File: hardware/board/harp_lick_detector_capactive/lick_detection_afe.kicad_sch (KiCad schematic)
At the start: 38 parts, among them J1 Conn_Coaxial, J3 Conn_Triaxial, U13 ADS7049, U6 LTC6263, U7 LTC6268xS8-10, U8 REF3433QDBVRQ1

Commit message: update footprints; populate bom
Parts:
- C22, C23, C27, C29: Link https://www.digikey.com/en/products/detail/murata-electronics/GRM188R61E106KA73J/9887674 -> https://www.digikey.com/en/products/detail/murata-electronics/GRM188R61E106KA73D/9867943; Manufacturer Number GRM188R61E106KA73J -> GRM188R61E106KA73D; Rated Voltage 10 -> 25V
- C28: footprint Capacitor_SMD:C_0402_1005Metric_Pad0.74x0.62mm_HandSolder -> Capacitor_SMD:C_0402_1005Metric
- R15: Link (none) -> https://www.digikey.com/en/products/detail/yageo/RT0402FRE0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; Manufacturer (none) -> Yageo; Manufacturer Number (none) -> RT0402FRE07100RL; Tolerance (none) -> 1%
- U7: Link (none) -> https://www.digikey.com/en/products/detail/analog-devices-i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; Manufacturer (none) -> Analog Devices Inc.; Manufacturer Number (none) -> LTC6268IS8-10#PBF
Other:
- note added: "TODO: J1 TVS Diode for static protection."
- company: (none) -> The Allen Institute for Neural Dynamics
- title: (none) -> Lickety Split Capacitive Lick Detector
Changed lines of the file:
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@@
 (kicad_sch (version 20230121) (generator eeschema)
   (paper "A4")
+  (title_block
+    (title "Lickety Split Capacitive Lick Detector")
+    (date "2023-09-01")
+    (rev "0.5")
+    (company "The Allen Institute for Neural Dynamics")
+  )
   (junction (at 247.65 28.575) (diameter 0) (color 0 0 0 0)
   )
@@
     (at 20.955 83.185 0)
     (effects (font (size 1.27 1.27)) (justify left bottom))
+  )
+  (text "TODO: J1 TVS Diode for static protection." (at 201.93 140.335 0)
+    (effects (font (size 2 2) (thickness 0.4) bold) (justify left bottom))
   )
   (text "TODO: consider common mode choke for connector inputs.\n3-line: EXC-16CT350U"
@@
       (effects (font (size 1.27 1.27)) hide)
     )
+    (property "Manufacturer Number" "LTC6268IS8-10#PBF" (at 109.22 97.155 0)
+      (effects (font (size 1.27 1.27)) hide)
+    )
+    (property "Manufacturer" "Analog Devices Inc." (at 109.22 97.155 0)
+      (effects (font (size 1.27 1.27)) hide)
+    )
+    (property "Link" "https://www.digikey.com/en/products/detail/analog-devices-inc/LTC6268IS8-10-PBF/5253539" (at 109.22 97.155 0)
+      (effects (font (size 1.27 1.27)) hide)
+    )
     (pin "1")
     (pin "2")
@@
       (effects (font (size 1.27 1.27)) hide)
     )
-    (property "Datasheet" "~" (at 92.71 97.155 0)
+    (property "Datasheet" "n/a" (at 92.71 97.155 0)
+      (effects (font (size 1.27 1.27)) hide)
+    )
+    (property "Link" "https://www.digikey.com/en/products/detail/yageo/RT0402FRE07100RL/1071699" (at 92.71 97.155 0)
+      (effects (font (size 1.27 1.27)) hide)
+    )
+    (property "Manufacturer" "Yageo" (at 92.71 97.155 0)
+      (effects (font (size 1.27 1.27)) hide)
+    )
+    (property "Manufacturer Number" "RT0402FRE07100RL" (at 92.71 97.155 0)
+      (effects (font (size 1.27 1.27)) hide)
+    )
+    (property "Tolerance" "1%" (at 92.71 97.155 0)
       (effects (font (size 1.27 1.27)) hide)
     )
@@
       (effects (font (size 1.27 1.27)) hide)
     )
-    (property "Datasheet" "https://search.murata.co.jp/Ceramy/image/img/A01X/G101/ENG/GRM188R61E106KA73-01A.pdf" (at 125.73 179.07 0)
-      (effects (font (size 1.27 1.27)) hide)
-    )
-    (property "Link" "https://www.digikey.com/en/products/detail/murata-electronics/GRM188R61E106KA73J/9887674" (at 125.73 179.07 0)
+    (property "Datasheet" "https://search.murata.co.jp/Ceramy/image/img/A01X/G101/ENG/GRM188R61E106KA73-01.pdf" (at 125.73 179.07 0)
+      (effects (font (size 1.27 1.27)) hide)
+    )
+    (property "Link" "https://www.digikey.com/en/products/detail/murata-electronics/GRM188R61E106KA73D/9867943" (at 125.73 179.07 0)
       (effects (font (size 1.27 1.27)) hide)
     )
@@
       (effects (font (size 1.27 1.27)) hide)
     )
-    (property "Manufacturer Number" "GRM188R61E106KA73J" (at 125.73 179.07 0)
-      (effects (font (size 1.27 1.27)) hide)
-    )
-    (property "Rated Voltage" "10" (at 125.73 179.07 0)
+    (property "Manufacturer Number" "GRM188R61E106KA73D" (at 125.73 179.07 0)
+      (effects (font (size 1.27 1.27)) hide)
+    )
+    (property "Rated Voltage" "25V" (at 125.73 179.07 0)
       (effects (font (size 1.27 1.27)) hide)
     )
@@
       (effects (font (size 1.27 1.27)) (justify left))
     )
-    (property "Footprint" "Capacitor_SMD:C_0402_1005Metric_Pad0.74x0.62mm_HandSolder" (at 115.8748 175.26 0)
+    (property "Footprint" "Capacitor_SMD:C_0402_1005Metric" (at 115.8748 175.26 0)
       (effects (font (size 1.27 1.27)) hide)
     )
@@
       (effects (font (size 1.27 1.27)) hide)
     )
-    (property "Datasheet" "https://search.murata.co.jp/Ceramy/image/img/A01X/G101/ENG/GRM188R61E106KA73-01A.pdf" (at 32.385 172.72 0)
-      (effects (font (size 1.27 1.27)) hide)
-    )
-    (property "Link" "https://www.digikey.com/en/products/detail/murata-electronics/GRM188R61E106KA73J/9887674" (at 32.385 172.72 0)
+    (property "Datasheet" "https://search.murata.co.jp/Ceramy/image/img/A01X/G101/ENG/GRM188R61E106KA73-01.pdf" (at 32.385 172.72 0)
+      (effects (font (size 1.27 1.27)) hide)
+    )
+    (property "Link" "https://www.digikey.com/en/products/detail/murata-electronics/GRM188R61E106KA73D/9867943" (at 32.385 172.72 0)
       (effects (font (size 1.27 1.27)) hide)
     )
@@
       (effects (font (size 1.27 1.27)) hide)
     )
-    (property "Manufacturer Number" "GRM188R61E106KA73J" (at 32.385 172.72 0)
-      (effects (font (size 1.27 1.27)) hide)
-    )
-    (property "Rated Voltage" "10" (at 32.385 172.72 0)
+    (property "Manufacturer Number" "GRM188R61E106KA73D" (at 32.385 172.72 0)
+      (effects (font (size 1.27 1.27)) hide)
+    )
+    (property "Rated Voltage" "25V" (at 32.385 172.72 0)
       (effects (font (size 1.27 1.27)) hide)
     )
@@
       (effects (font (size 1.27 1.27)) hide)
     )
-    (property "Datasheet" "https://search.murata.co.jp/Ceramy/image/img/A01X/G101/ENG/GRM188R61E106KA73-01A.pdf" (at 32.385 184.15 0)
-      (effects (font (size 1.27 1.27)) hide)
-    )
-    (property "Link" "https://www.digikey.com/en/products/detail/murata-electronics/GRM188R61E106KA73J/9887674" (at 32.385 184.15 0)
+    (property "Datasheet" "https://search.murata.co.jp/Ceramy/image/img/A01X/G101/ENG/GRM188R61E106KA73-01.pdf" (at 32.385 184.15 0)
+      (effects (font (size 1.27 1.27)) hide)
+    )
+    (property "Link" "https://www.digikey.com/en/products/detail/murata-electronics/GRM188R61E106KA73D/9867943" (at 32.385 184.15 0)
       (effects (font (size 1.27 1.27)) hide)
     )
@@
       (effects (font (size 1.27 1.27)) hide)
     )
-    (property "Manufacturer Number" "GRM188R61E106KA73J" (at 32.385 184.15 0)
-      (effects (font (size 1.27 1.27)) hide)
-    )
-    (property "Rated Voltage" "10" (at 32.385 184.15 0)
+    (property "Manufacturer Number" "GRM188R61E106KA73D" (at 32.385 184.15 0)
+      (effects (font (size 1.27 1.27)) hide)
+    )
+    (property "Rated Voltage" "25V" (at 32.385 184.15 0)
       (effects (font (size 1.27 1.27)) hide)
     )
@@
       (effects (font (size 1.27 1.27)) hide)
     )
-    (property "Datasheet" "https://search.murata.co.jp/Ceramy/image/img/A01X/G101/ENG/GRM188R61E106KA73-01A.pdf" (at 99.06 179.07 0)
-      (effects (font (size 1.27 1.27)) hide)
-    )
-    (property "Link" "https://www.digikey.com/en/products/detail/murata-electronics/GRM188R61E106KA73J/9887674" (at 99.06 179.07 0)
+    (property "Datasheet" "https://search.murata.co.jp/Ceramy/image/img/A01X/G101/ENG/GRM188R61E106KA73-01.pdf" (at 99.06 179.07 0)
+      (effects (font (size 1.27 1.27)) hide)
+    )
+    (property "Link" "https://www.digikey.com/en/products/detail/murata-electronics/GRM188R61E106KA73D/9867943" (at 99.06 179.07 0)
       (effects (font (size 1.27 1.27)) hide)
     )
@@
       (effects (font (size 1.27 1.27)) hide)
     )
-    (property "Manufacturer Number" "GRM188R61E106KA73J" (at 99.06 179.07 0)
-      (effects (font (size 1.27 1.27)) hide)
-    )
-    (property "Rated Voltage" "10" (at 99.06 179.07 0)
-      (effects (font (size 1.27 1.27)) hide)
-    )
+    (property "Manufacturer Number" "GRM188R61E106KA73D" (at 99.06 179.07 0)
+      (effects (font (size 1.27 1.27)) hide)
+    )
+    (property "Rated Voltage" "25V" (at 99.06 179.07 0)
+      (effects (font (size 1.27 1.27)) hide)
+    )

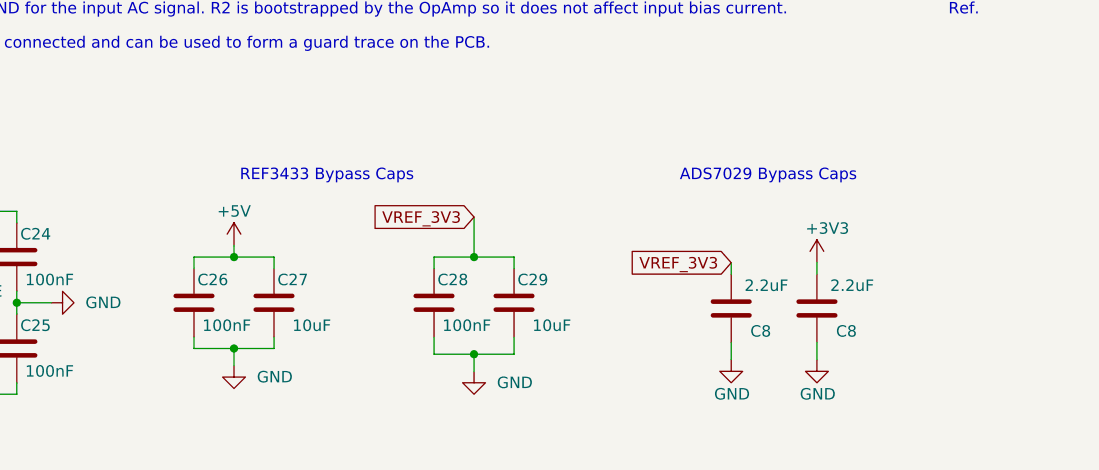
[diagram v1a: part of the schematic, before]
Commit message: consolidate components; add extra decoupling cap to voltage divider
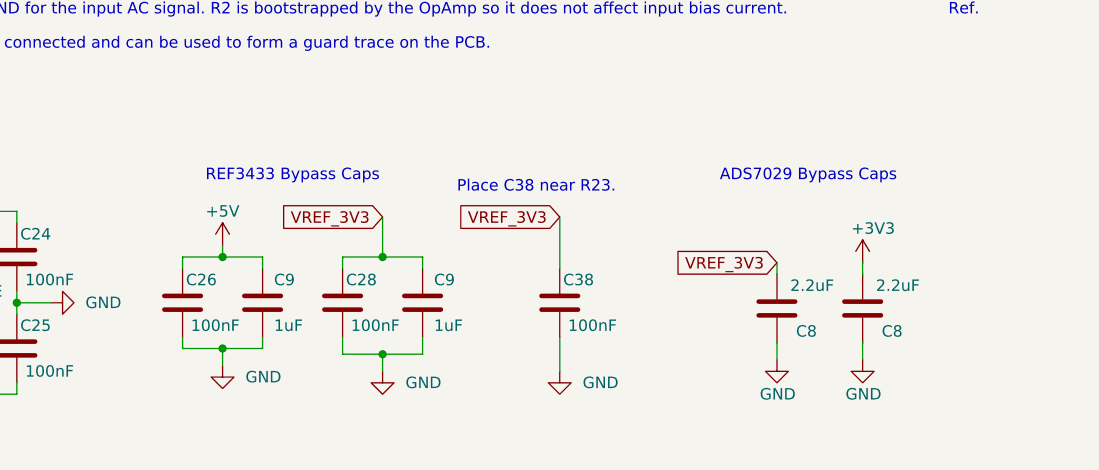
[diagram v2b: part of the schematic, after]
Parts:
- removed C27, C29: 10uF, Capacitor_SMD:C_0603_1608Metric, symbol Device:C
- added C38: 100nF, Capacitor_SMD:C_0402_1005Metric, symbol Device:C
- added C9 (x2): 1uF, Capacitor_SMD:C_0402_1005Metric, symbol Device:C
- C22, C23: footprint Capacitor_SMD:C_0603_1608Metric -> Capacitor_SMD:C_0805_2012Metric; Link https://www.digikey.com/en/products/detail/murata-electronics/GRM188R61E106KA73D/9867943 -> https://www.digikey.com/en/products/detail/murata-electronics/GRM21BZ71E106KE15L/13904911; Manufacturer Number GRM188R61E106KA73D -> GRM21BZ71E106KE15L; Temperature Coefficient X5R -> X7R; Tolerance 10% -> (none)
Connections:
- net +5V: now also C9.1
- net GND: now also C38.1, C9.2, C9.2
- net VREF_3V3: now also C38.2, C9.1
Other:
- note added: "Place C38 near R23."
- moved on the sheet: C26, C28, C8

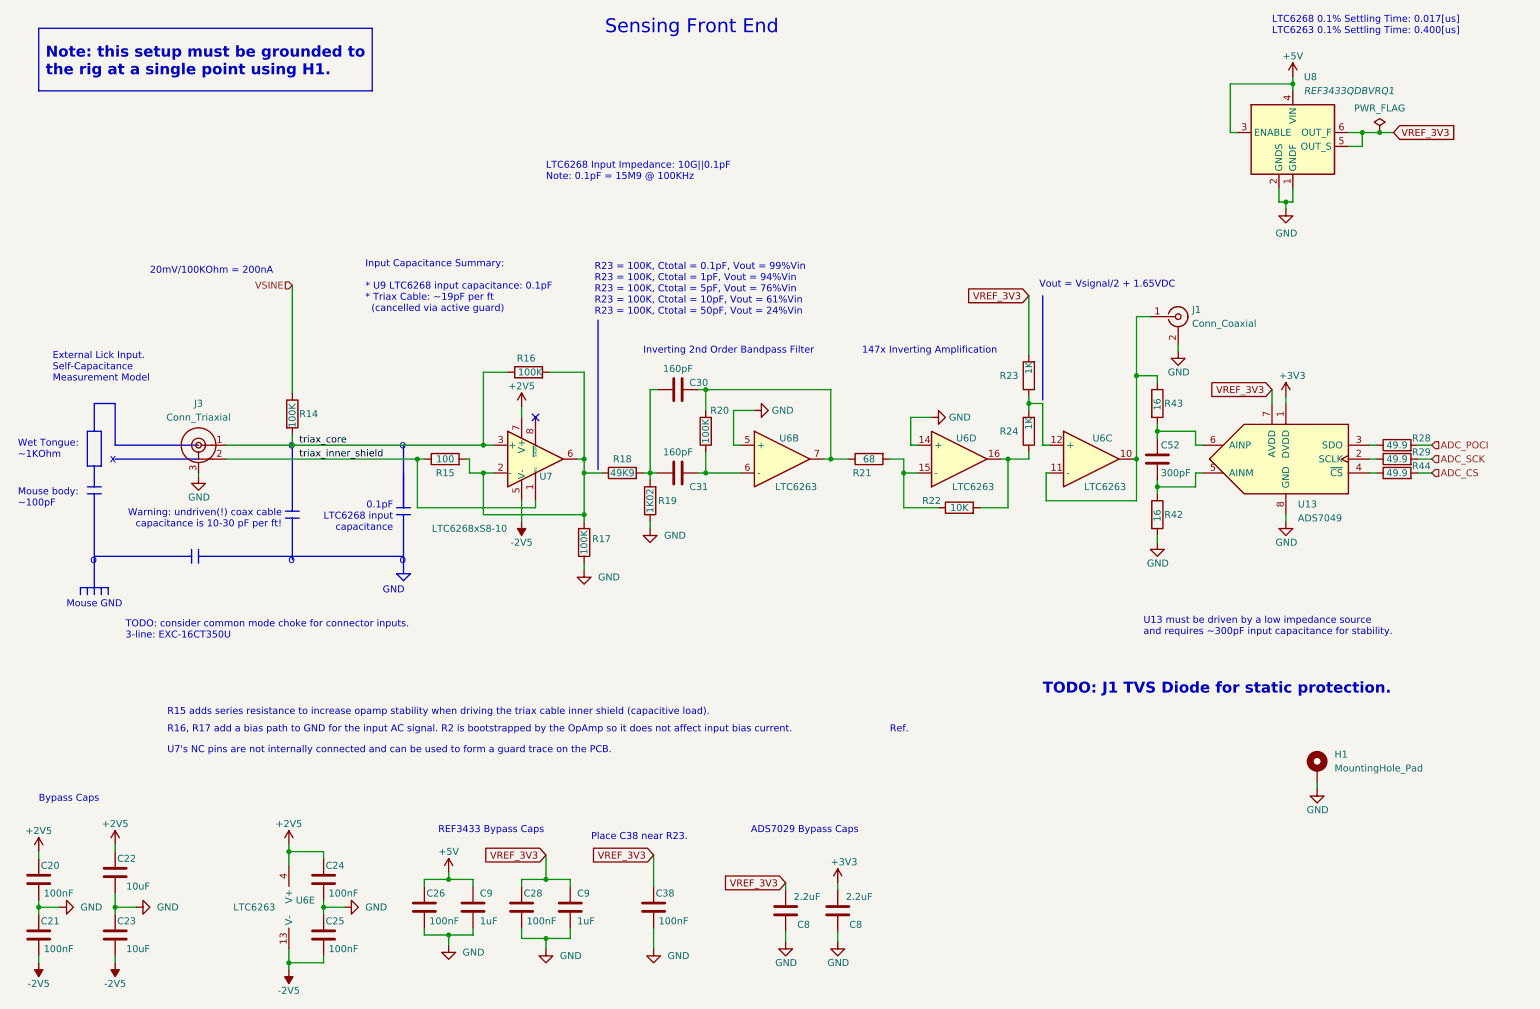
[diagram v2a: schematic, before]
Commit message: add tvs diodes; remove run pullup; finish trace guard
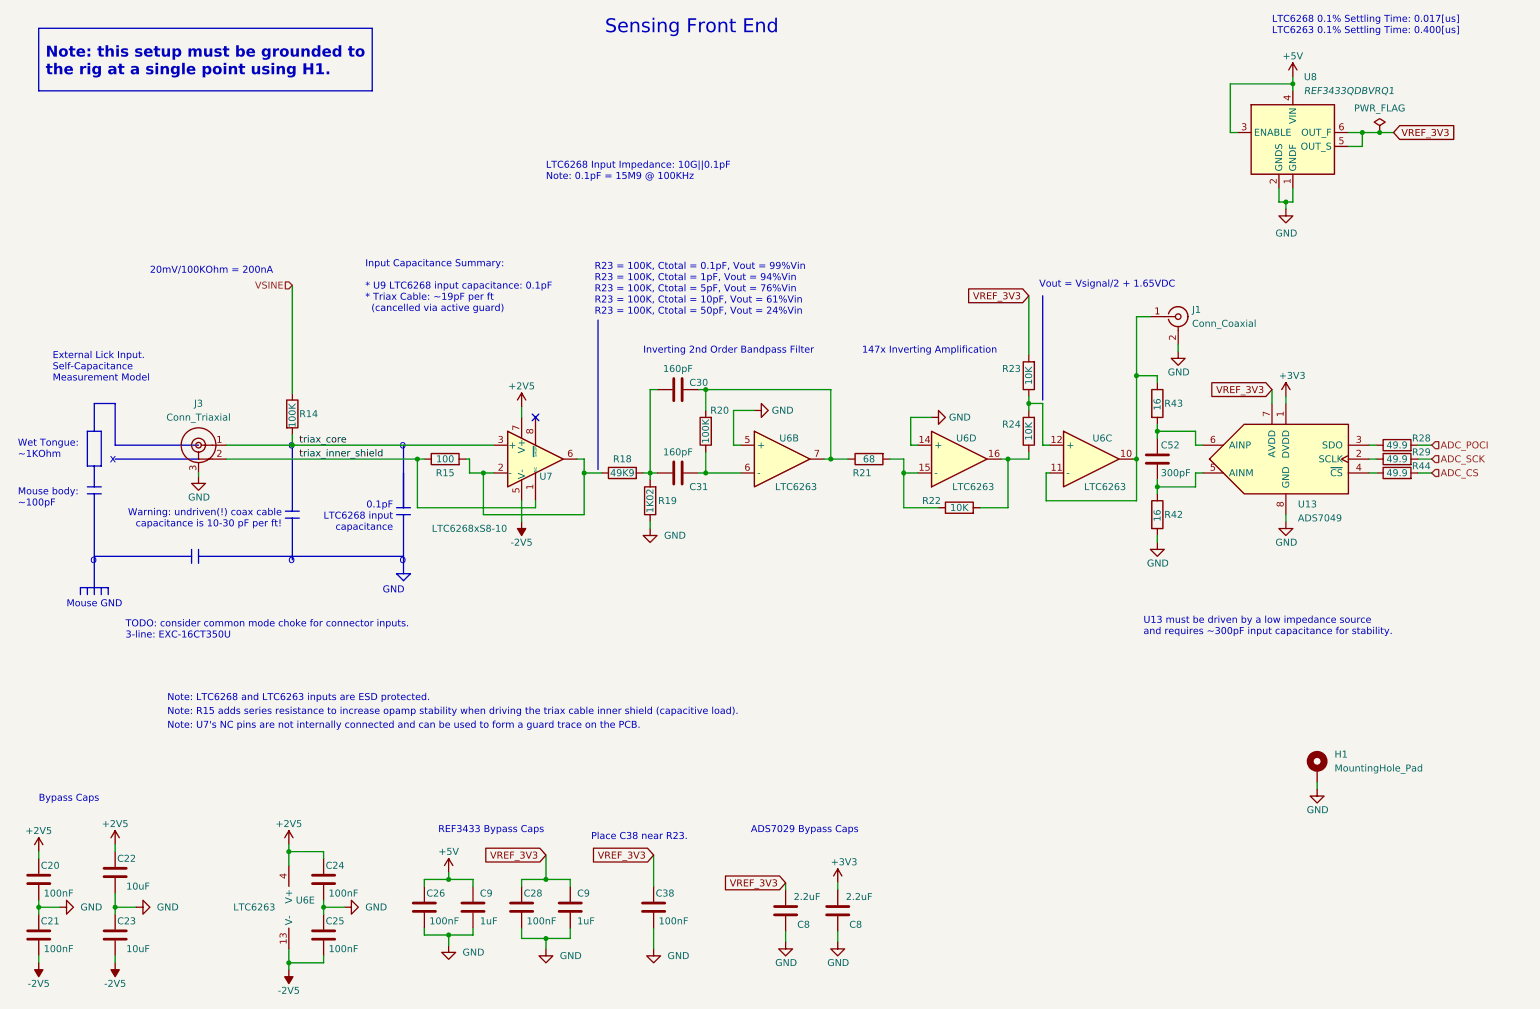
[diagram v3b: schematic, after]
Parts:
- removed R16: 100K, Resistor_SMD:R_0805_2012Metric, symbol Device:R
- removed R17: 100K, Resistor_SMD:R_0402_1005Metric, symbol Device:R
- R14: footprint Resistor_SMD:R_0805_2012Metric -> Resistor_SMD:R_1206_3216Metric; Link https://www.digikey.com/en/products/detail/panasonic-electr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 -> https://www.digikey.com/en/products/detail/yageo/RC0402FR-1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; Manufacturer Panasonic Electronic Components -> Yageo; Manufacturer Number ERA-6AEB104V -> RC0402FR-13100KL; Tolerance 0.1% -> 1%
- R23, R24: value 1K -> 10K; Link https://www.digikey.com/en/products/detail/yageo/RT0402BRD071KL/1069118 -> https://www.digikey.com/en/products/detail/yageo/RT0402BRD0710KL/1068998; Manufacturer Number RT0402BRD071KL -> RT0402BRD0710KL; Temperature Coefficient (none) -> 25ppm/C
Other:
- note added: "Note: LTC6268 and LTC6263 inputs are ESD protected."
- note added: "Note: R15 adds series resistance to increase opamp stability when driving the triax cable inner shield (capacitive load)."
- note added: "Note: U7's NC pins are not internally connected and can be used to form a guard trace on the PCB."
- note removed: "R15 adds series resistance to increase opamp stability when driving the triax cable inner shield (capacitive load)."
- note removed: "R16, R17 add a bias path to GND for the input AC signal. R2 is bootstrapped by the OpAmp so it does not affect input bias current."
- note removed: "Ref."
- note removed: "TODO: J1 TVS Diode for static protection."
- note removed: "U7's NC pins are not internally connected and can be used to form a guard trace on the PCB."

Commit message: update ads7049 pinout
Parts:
- R14: Link https://www.digikey.com/en/products/detail/yageo/RC0402FR-1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 -> https://www.digikey.com/en/products/detail/yageo/RT1206FRE0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; Manufacturer Number RC0402FR-13100KL -> https://www.digikey.com/en/products/detail/yageo/RT1206FRE0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
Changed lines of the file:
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@@
       (effects (font (size 1.27 1.27)) hide)
     )
-    (property "Datasheet" "https://www.yageo.com/upload/media/product/productsearch/datasheet/rchip/PYu-RC_Group_51_RoHS_L_12.pdf" (at 64.77 88.9 0)
+    (property "Datasheet" "n/a" (at 64.77 88.9 0)
       (effects (font (size 1.27 1.27)) hide)
     )
-    (property "Link" "https://www.digikey.com/en/products/detail/yageo/RC0402FR-13100KL/13546624" (at 64.77 88.9 0)
+    (property "Link" "https://www.digikey.com/en/products/detail/yageo/RT1206FRE07100KL/1082857" (at 64.77 88.9 0)
       (effects (font (size 1.27 1.27)) hide)
     )
@@
       (effects (font (size 1.27 1.27)) hide)
     )
-    (property "Manufacturer Number" "RC0402FR-13100KL" (at 64.77 88.9 0)
+    (property "Manufacturer Number" "https://www.digikey.com/en/products/detail/yageo/RT1206FRE07100KL/1082857" (at 64.77 88.9 0)
       (effects (font (size 1.27 1.27)) hide)
     )
